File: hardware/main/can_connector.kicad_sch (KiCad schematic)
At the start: 1 part

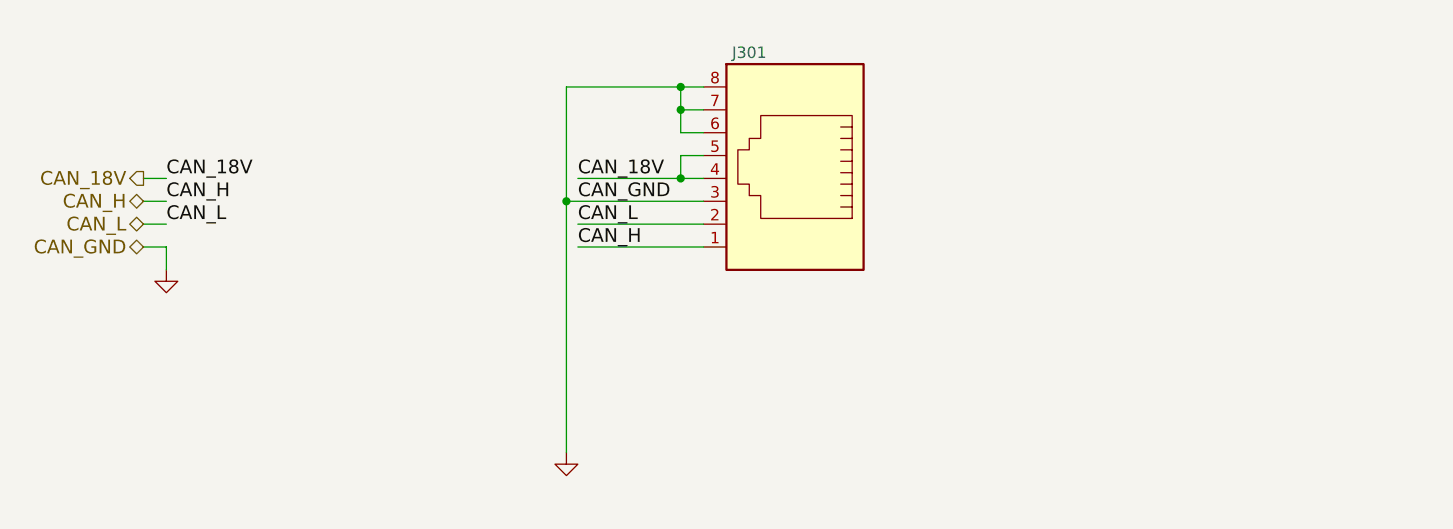
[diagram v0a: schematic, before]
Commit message: Schematics: finalize Analog Snubber and Supplies
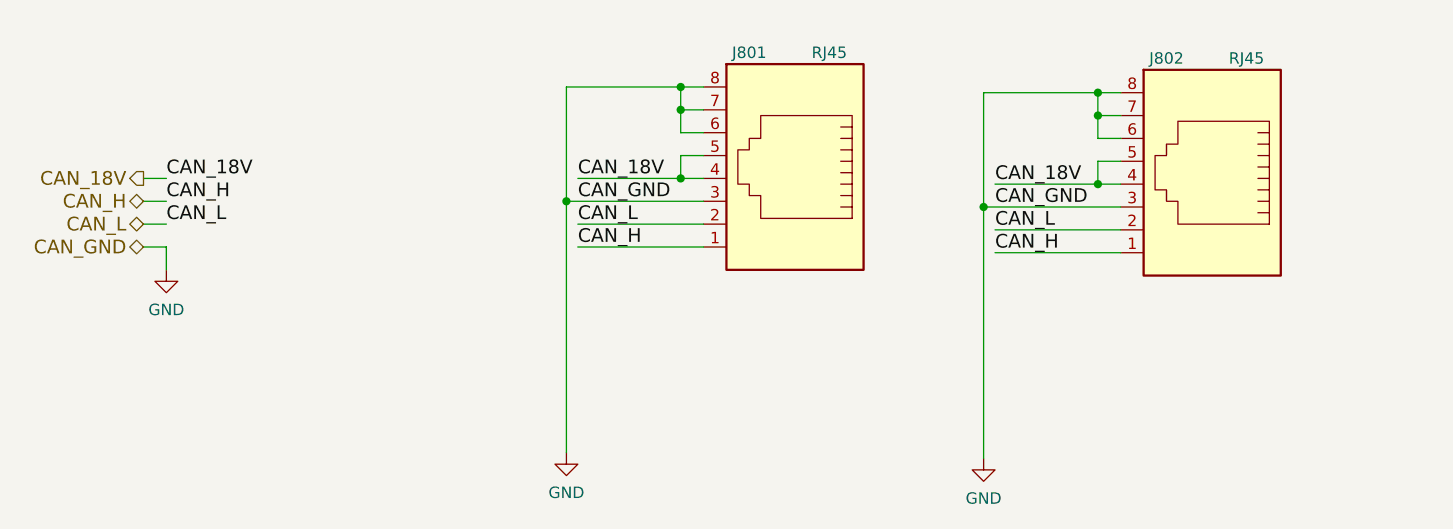
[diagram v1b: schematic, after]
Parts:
- added J802: RJ45, symbol Connector:RJ45
- J801: renamed from J301; value ~ -> RJ45
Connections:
- net CAN_18V: now also J802.4, J802.5
- net CAN_H: now also J802.1
- net CAN_L: now also J802.2
- net GND: now also J802.3, J802.6, J802.7, J802.8
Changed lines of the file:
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@@
   (junction (at 138.43 86.36) (diameter 0) (color 0 0 0 0)
   )
+  (junction (at 184.785 76.835) (diameter 0) (color 0 0 0 0)
+  )
+  (junction (at 172.085 89.535) (diameter 0) (color 0 0 0 0)
+  )
   (junction (at 138.43 78.74) (diameter 0) (color 0 0 0 0)
   )
   (junction (at 138.43 76.2) (diameter 0) (color 0 0 0 0)
   )
+  (junction (at 184.785 86.995) (diameter 0) (color 0 0 0 0)
+  )
   (junction (at 125.73 88.9) (diameter 0) (color 0 0 0 0)
   )
+  (junction (at 184.785 79.375) (diameter 0) (color 0 0 0 0)
+  )
+  (wire (pts (xy 172.085 89.535) (xy 187.325 89.535))
+    (stroke (width 0) (type default) (color 0 0 0 0))
+  )
+  (wire (pts (xy 184.785 84.455) (xy 184.785 86.995))
+    (stroke (width 0) (type default) (color 0 0 0 0))
+  )
   (wire (pts (xy 81.28 91.44) (xy 78.74 91.44))
     (stroke (width 0) (type default) (color 0 0 0 0))
@@
     (stroke (width 0) (type default) (color 0 0 0 0))
   )
+  (wire (pts (xy 172.085 89.535) (xy 172.085 117.475))
+    (stroke (width 0) (type default) (color 0 0 0 0))
+  )
+  (wire (pts (xy 173.355 92.075) (xy 187.325 92.075))
+    (stroke (width 0) (type default) (color 0 0 0 0))
+  )
   (wire (pts (xy 138.43 83.82) (xy 138.43 86.36))
     (stroke (width 0) (type default) (color 0 0 0 0))
@@
     (stroke (width 0) (type default) (color 0 0 0 0))
   )
+  (wire (pts (xy 187.325 94.615) (xy 173.355 94.615))
+    (stroke (width 0) (type default) (color 0 0 0 0))
+  )
   (wire (pts (xy 127 86.36) (xy 138.43 86.36))
     (stroke (width 0) (type default) (color 0 0 0 0))
@@
     (stroke (width 0) (type default) (color 0 0 0 0))
   )
+  (wire (pts (xy 187.325 79.375) (xy 184.785 79.375))
+    (stroke (width 0) (type default) (color 0 0 0 0))
+  )
+  (wire (pts (xy 187.325 76.835) (xy 184.785 76.835))
+    (stroke (width 0) (type default) (color 0 0 0 0))
+  )
+  (wire (pts (xy 173.355 86.995) (xy 184.785 86.995))
+    (stroke (width 0) (type default) (color 0 0 0 0))
+  )
+  (wire (pts (xy 184.785 76.835) (xy 172.085 76.835))
+    (stroke (width 0) (type default) (color 0 0 0 0))
+  )
+  (wire (pts (xy 184.785 81.915) (xy 184.785 79.375))
+    (stroke (width 0) (type default) (color 0 0 0 0))
+  )
+  (wire (pts (xy 172.085 76.835) (xy 172.085 89.535))
+    (stroke (width 0) (type default) (color 0 0 0 0))
+  )
+  (wire (pts (xy 184.785 86.995) (xy 187.325 86.995))
+    (stroke (width 0) (type default) (color 0 0 0 0))
+  )
   (wire (pts (xy 140.97 78.74) (xy 138.43 78.74))
     (stroke (width 0) (type default) (color 0 0 0 0))
@@
     (stroke (width 0) (type default) (color 0 0 0 0))
   )
+  (wire (pts (xy 187.325 81.915) (xy 184.785 81.915))
+    (stroke (width 0) (type default) (color 0 0 0 0))
+  )
+  (wire (pts (xy 184.785 79.375) (xy 184.785 76.835))
+    (stroke (width 0) (type default) (color 0 0 0 0))
+  )
   (wire (pts (xy 140.97 76.2) (xy 138.43 76.2))
     (stroke (width 0) (type default) (color 0 0 0 0))
@@
     (stroke (width 0) (type default) (color 0 0 0 0))
   )
+  (wire (pts (xy 187.325 84.455) (xy 184.785 84.455))
+    (stroke (width 0) (type default) (color 0 0 0 0))
+  )
   (wire (pts (xy 138.43 76.2) (xy 125.73 76.2))
     (stroke (width 0) (type default) (color 0 0 0 0))
@@
     (effects (font (size 1.524 1.524)) (justify left bottom))
   )
+  (label "CAN_GND" (at 173.355 89.535 0)
+    (effects (font (size 1.524 1.524)) (justify left bottom))
+  )
   (label "CAN_L" (at 127 91.44 0)
     (effects (font (size 1.524 1.524)) (justify left bottom))
@@
     (effects (font (size 1.524 1.524)) (justify left bottom))
   )
+  (label "CAN_18V" (at 173.355 86.995 0)
+    (effects (font (size 1.524 1.524)) (justify left bottom))
+  )
   (label "CAN_18V" (at 81.28 86.36 0)
+    (effects (font (size 1.524 1.524)) (justify left bottom))
+  )
+  (label "CAN_L" (at 173.355 92.075 0)
+    (effects (font (size 1.524 1.524)) (justify left bottom))
+  )
+  (label "CAN_H" (at 173.355 94.615 0)
     (effects (font (size 1.524 1.524)) (justify left bottom))
   )
@@
   (symbol (lib_id "Connector:RJ45") (at 151.13 86.36 0) (mirror y) (unit 1)
     (in_bom yes) (on_board yes)
-    (property "Reference" "J301" (id 0) (at 146.05 72.39 0))
-    (property "Value" "~" (id 1) (at 154.94 72.39 0))
+    (property "Reference" "J801" (id 0) (at 146.05 72.39 0))
+    (property "Value" "RJ45" (id 1) (at 154.94 72.39 0))
     (property "Footprint" "" (id 2) (at 151.13 86.36 0)
       (effects (font (size 1.27 1.27)) hide)
@@
     (pin "8")
   )
+  (symbol (lib_id "power:GND") (at 172.085 117.475 0) (unit 1)
+    (in_bom yes) (on_board yes) (fields_autoplaced)
+    (property "Reference" "#PWR0803" (id 0) (at 172.085 123.825 0)
+      (effects (font (size 1.27 1.27)) hide)
+    )
+    (property "Value" "GND" (id 1) (at 172.085 121.9184 0))
+    (property "Footprint" "" (id 2) (at 172.085 117.475 0)
+      (effects (font (size 1.27 1.27)) hide)
+    )
+    (property "Datasheet" "" (id 3) (at 172.085 117.475 0)
+      (effects (font (size 1.27 1.27)) hide)
+    )
+    (pin "1")
+  )
+  (symbol (lib_id "Connector:RJ45") (at 197.485 86.995 0) (mirror y) (unit 1)
+    (in_bom yes) (on_board yes)
+    (property "Reference" "J802" (id 0) (at 192.405 73.025 0))
+    (property "Value" "RJ45" (id 1) (at 201.295 73.025 0))
+    (property "Footprint" "" (id 2) (at 197.485 86.995 0)
+      (effects (font (size 1.27 1.27)) hide)
+    )
+    (property "Datasheet" "" (id 3) (at 197.485 86.995 0)
+      (effects (font (size 1.27 1.27)) hide)
+    )
+    (pin "1")
+    (pin "2")
+    (pin "3")
+    (pin "4")
+    (pin "5")
+    (pin "6")
+    (pin "7")
+    (pin "8")
+  )
+  (symbol (lib_id "power:GND") (at 81.28 96.52 0) (unit 1)
+    (in_bom yes) (on_board yes) (fields_autoplaced)
+    (property "Reference" "#PWR0801" (id 0) (at 81.28 102.87 0)
+      (effects (font (size 1.27 1.27)) hide)
+    )
+    (property "Value" "GND" (id 1) (at 81.28 100.9634 0))
+    (property "Footprint" "" (id 2) (at 81.28 96.52 0)
+      (effects (font (size 1.27 1.27)) hide)
+    )
+    (property "Datasheet" "" (id 3) (at 81.28 96.52 0)
+      (effects (font (size 1.27 1.27)) hide)
+    )
+    (pin "1")
+  )
   (symbol (lib_id "power:GND") (at 125.73 116.84 0) (unit 1)
-    (in_bom yes) (on_board yes)
-    (property "Reference" "#PWR0302" (id 0) (at 125.73 123.19 0)
-      (effects (font (size 1.27 1.27)) hide)
-    )
-    (property "Value" "~" (id 1) (at 127 121.92 0))
+    (in_bom yes) (on_board yes) (fields_autoplaced)
+    (property "Reference" "#PWR0802" (id 0) (at 125.73 123.19 0)
+      (effects (font (size 1.27 1.27)) hide)
+    )
+    (property "Value" "GND" (id 1) (at 125.73 121.2834 0))
     (property "Footprint" "" (id 2) (at 125.73 116.84 0)
       (effects (font (size 1.27 1.27)) hide)
@@
       (effects (font (size 1.27 1.27)) hide)
     )
-    (pin "1")
-  )
-  (symbol (lib_id "power:GND") (at 81.28 96.52 0) (unit 1)
-    (in_bom yes) (on_board yes)
-    (property "Reference" "#PWR0301" (id 0) (at 81.28 102.87 0)
-      (effects (font (size 1.27 1.27)) hide)
-    )
-    (property "Value" "~" (id 1) (at 82.55 101.6 0))
-    (property "Footprint" "" (id 2) (at 81.28 96.52 0)
-      (effects (font (size 1.27 1.27)) hide)
-    )
-    (property "Datasheet" "" (id 3) (at 81.28 96.52 0)
-      (effects (font (size 1.27 1.27)) hide)
-    )

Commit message: Schematics: Sym table and libs updated
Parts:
- removed J801, J802: RJ45, symbol Connector:RJ45
- added J801, J802: RJ45_Shielded, symbol Connector:RJ45_Shielded
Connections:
- net CAN_18V: now also J801.4, J801.5, J802.4, J802.5
- net CAN_H: now also J801.1, J802.1
- net CAN_L: now also J801.2, J802.2
- net GND: now also J801.3, J801.6, J801.7, J801.8, J801.9 (SH), J802.3, J802.6, J802.7, J802.8, J802.9 (SH)

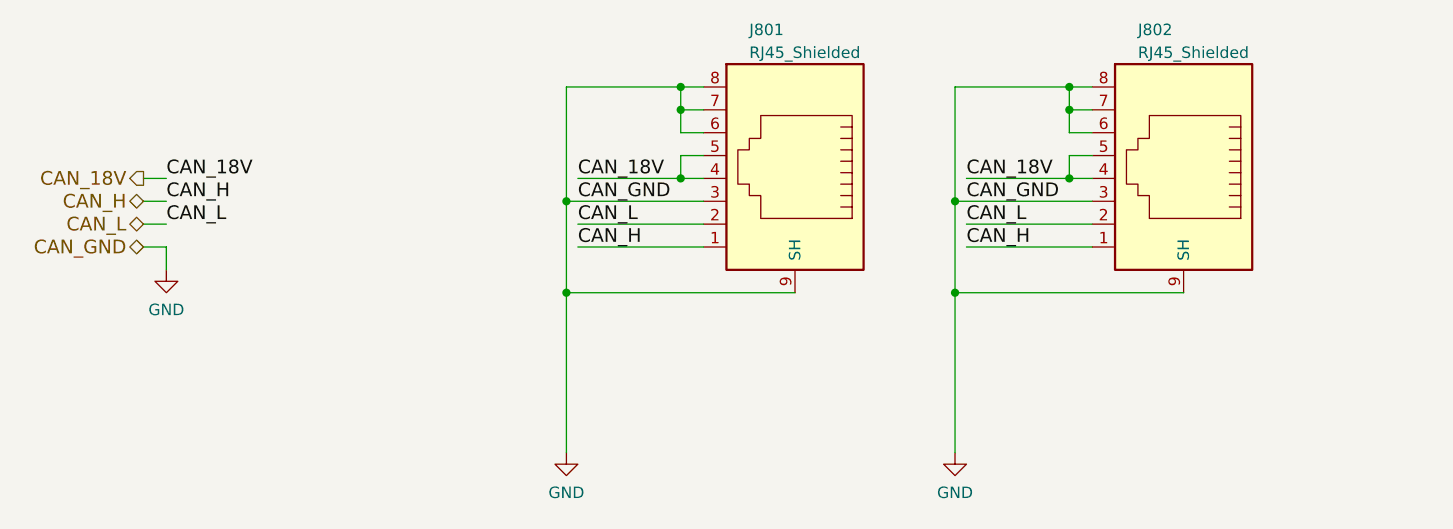
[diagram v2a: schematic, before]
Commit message: Schematics: Run DRC and fix errors and some warnings, also added Zenite kicad library repo as submodule
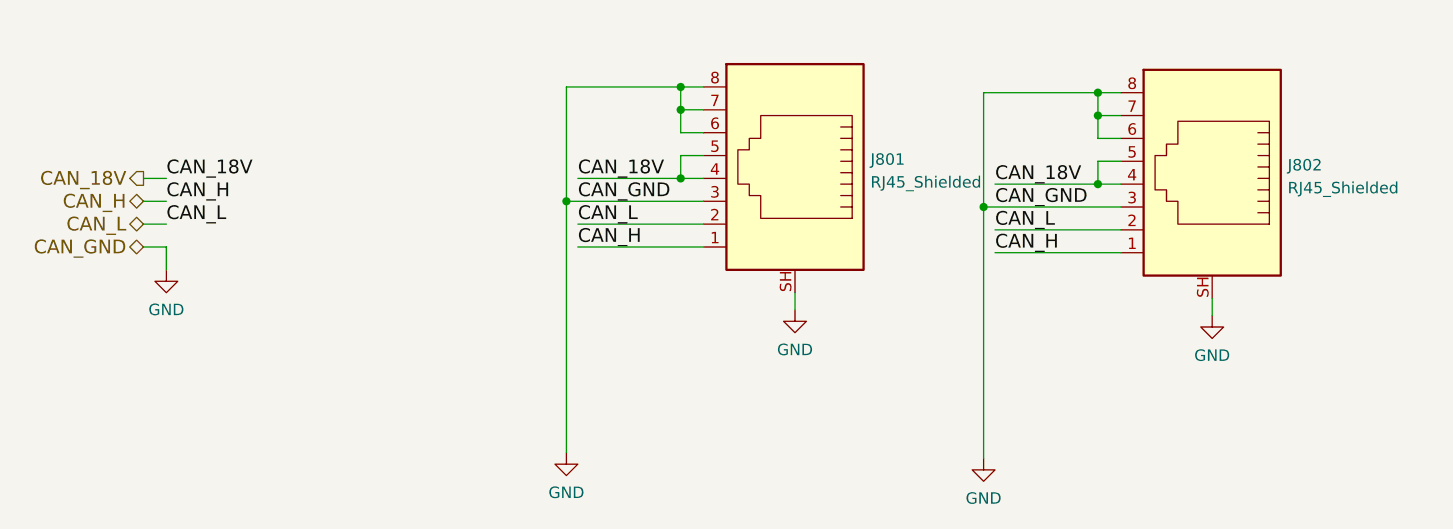
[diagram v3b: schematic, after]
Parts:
- J801, J802: footprint (none) -> Zenite:RJ45_YH59_01
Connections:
- net GND: now also J801.SH, J802.SH; no longer J801.9 (SH), J802.9 (SH)
